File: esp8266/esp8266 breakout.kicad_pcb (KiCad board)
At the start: 2 copper layers, 57.2 x 49.5 mm, 16 parts, among them IC1 DS18B20, P1 power, P3 ftdi, P4 dust, SW1 SW_PUSH, U1 esp8266, U2 AP1117D33

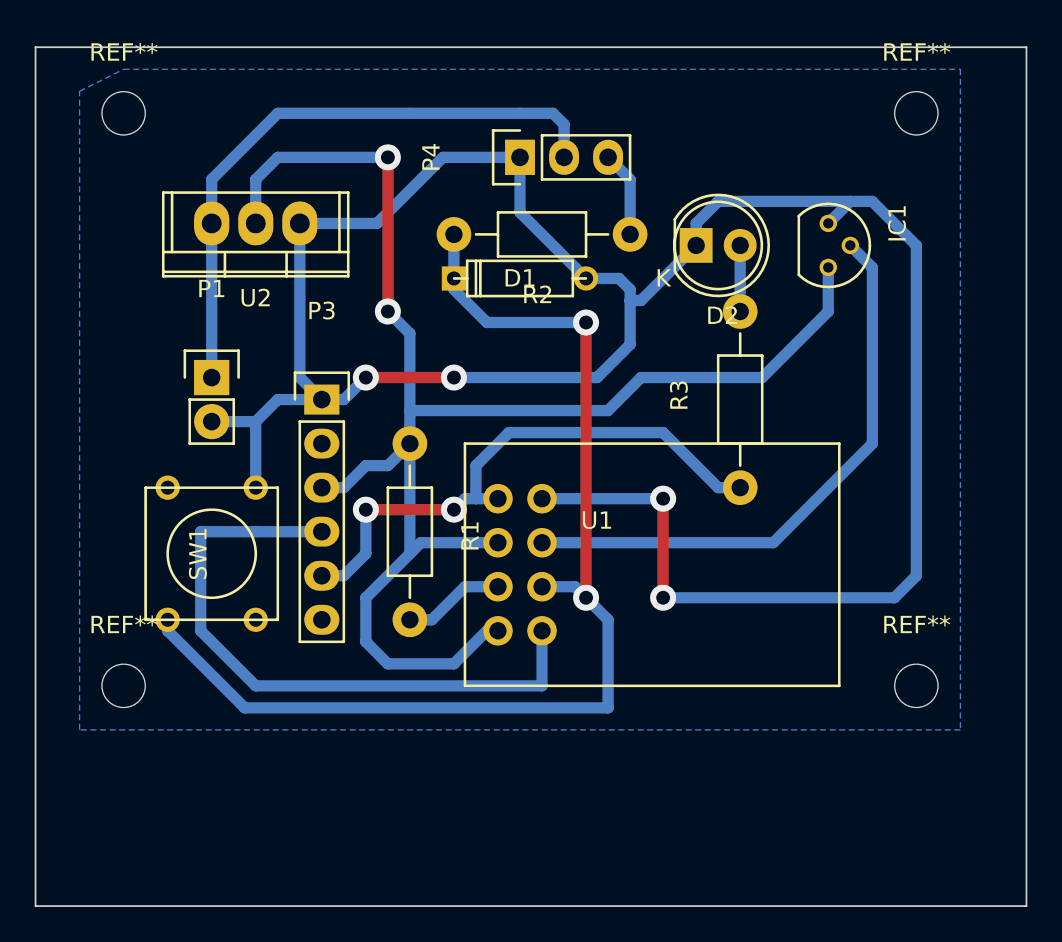
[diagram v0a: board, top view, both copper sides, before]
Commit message: all libs inside project
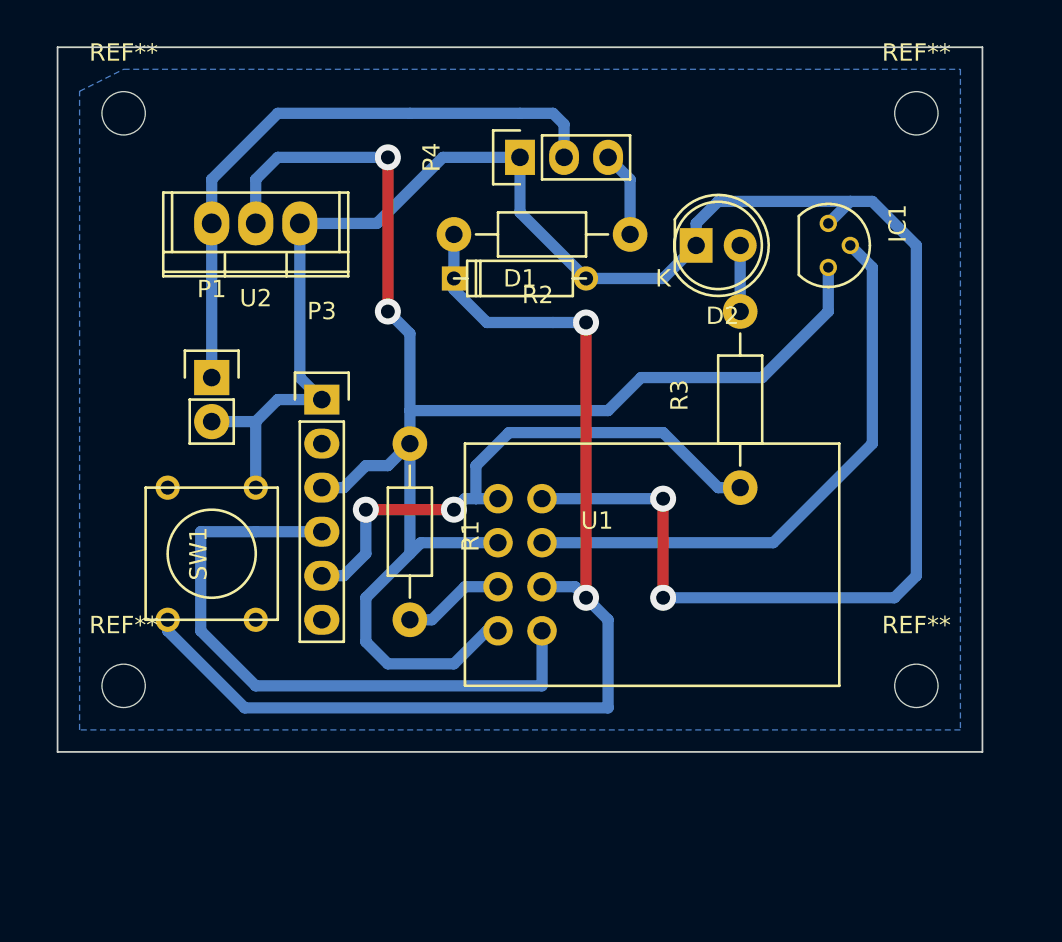
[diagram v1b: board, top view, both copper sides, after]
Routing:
- net GND: track 138.6 -> 115.6 mm, vias 4 -> 2
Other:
- board size 57.2 x 49.5 mm -> 53.3 x 40.6 mm
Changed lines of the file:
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@@
     (links 27)
     (no_connects 2)
-    (area 140.919999 52.019999 198.170001 101.650001)
+    (area 127.255001 39.695 200.453584 93.47418)
     (thickness 1.6)
-    (drawings 4)
-    (tracks 120)
+    (drawings 6)
+    (tracks 109)
     (zones 0)
     (modules 16)
@@
     (pad_drill 0.6)
     (pad_to_mask_clearance 0)
-    (aux_axis_origin 0 0)
+    (aux_axis_origin 146.05 88.9)
     (visible_elements FFFDFF7F)
     (pcbplotparams
@@
       (padsonsilk false)
       (subtractmaskfromsilk false)
-      (outputformat 1)
+      (outputformat 4)
       (mirror false)
       (drillshape 0)
@@
       (effects (font (size 1 1) (thickness 0.15)))
     )
-    (fp_text value MountingHole_2-5mm (at 0.09906 3.59918) (layer F.Fab)
+    (fp_text value MountingHole_2-5mm (at 0 -5.08) (layer F.Fab)
       (effects (font (size 1 1) (thickness 0.15)))
     )
@@
     (pad 1 thru_hole circle (at 0 0) (size 2.5 2.5) (drill 2.5) (layers))
   )
-  (gr_line (start 140.97 101.6) (end 140.97 52.07) (angle 90) (layer Edge.Cuts) (width 0.1))
-  (gr_line (start 198.12 101.6) (end 140.97 101.6) (angle 90) (layer Edge.Cuts) (width 0.1))
-  (gr_line (start 198.12 52.07) (end 198.12 101.6) (angle 90) (layer Edge.Cuts) (width 0.1))
-  (gr_line (start 140.97 52.07) (end 198.12 52.07) (angle 90) (layer Edge.Cuts) (width 0.1))
+  (gr_line (start 142.24 92.71) (end 142.24 52.07) (angle 90) (layer Edge.Cuts) (width 0.1))
+  (gr_line (start 195.58 92.71) (end 142.24 92.71) (angle 90) (layer Edge.Cuts) (width 0.1))
+  (gr_line (start 195.58 52.07) (end 195.58 92.71) (angle 90) (layer Edge.Cuts) (width 0.1))
+  (gr_line (start 142.24 52.07) (end 195.58 52.07) (angle 90) (layer Edge.Cuts) (width 0.1))
+  (dimension 33.02 (width 0.3) (layer F.SilkS)
+    (gr_text "33.020 mm" (at 133.905 72.39 90) (layer F.SilkS)
+      (effects (font (size 1.5 1.5) (thickness 0.3)))
+    )
+    (feature1 (pts (xy 146.05 55.88) (xy 132.555 55.88)))
+    (feature2 (pts (xy 146.05 88.9) (xy 132.555 88.9)))
+    (crossbar (pts (xy 135.255 88.9) (xy 135.255 55.88)))
+    (arrow1a (pts (xy 135.255 55.88) (xy 135.841421 57.006504)))
+    (arrow1b (pts (xy 135.255 55.88) (xy 134.668579 57.006504)))
+    (arrow2a (pts (xy 135.255 88.9) (xy 135.841421 87.773496)))
+    (arrow2b (pts (xy 135.255 88.9) (xy 134.668579 87.773496)))
+  )
+  (dimension 45.72 (width 0.3) (layer F.SilkS)
+    (gr_text "45.720 mm" (at 168.91 41.195) (layer F.SilkS)
+      (effects (font (size 1.5 1.5) (thickness 0.3)))
+    )
+    (feature1 (pts (xy 191.77 55.88) (xy 191.77 39.845)))
+    (feature2 (pts (xy 146.05 55.88) (xy 146.05 39.845)))
+    (crossbar (pts (xy 146.05 42.545) (xy 191.77 42.545)))
+    (arrow1a (pts (xy 191.77 42.545) (xy 190.643496 43.131421)))
+    (arrow1b (pts (xy 191.77 42.545) (xy 190.643496 41.958579)))
+    (arrow2a (pts (xy 146.05 42.545) (xy 147.176504 43.131421)))
+    (arrow2b (pts (xy 146.05 42.545) (xy 147.176504 41.958579)))
+  )
   (segment (start 178.435 71.12) (end 175.895 71.12) (width 0.65) (layer B.Cu) (net 1))
   (segment (start 178.435 71.12) (end 182.88 71.12) (width 0.65) (layer B.Cu) (net 1))
@@
   (segment (start 162.56 68.58) (end 162.56 73.025) (width 0.65) (layer B.Cu) (net 1))
   (segment (start 162.56 73.025) (end 162.56 74.93) (width 0.65) (layer B.Cu) (net 1))
-  (segment (start 175.26 66.675) (end 175.895 66.675) (width 0.65) (layer B.Cu) (net 2))
-  (segment (start 175.895 66.675) (end 179.07 63.5) (width 0.65) (layer B.Cu) (net 2))
+  (segment (start 172.72 65.405) (end 177.165 65.405) (width 0.65) (layer B.Cu) (net 2))
+  (segment (start 177.165 65.405) (end 179.07 63.5) (width 0.65) (layer B.Cu) (net 2))
+  (segment (start 191.77 63.5) (end 191.77 82.55) (width 0.65) (layer B.Cu) (net 2))
   (segment (start 190.5 83.82) (end 177.165 83.82) (width 0.65) (layer B.Cu) (net 2))
   (segment (start 187.96 60.96) (end 189.23 60.96) (width 0.65) (layer B.Cu) (net 2))
   (segment (start 189.23 60.96) (end 191.77 63.5) (width 0.65) (layer B.Cu) (net 2))
-  (segment (start 191.77 63.5) (end 191.77 82.55) (width 0.65) (layer B.Cu) (net 2))
   (segment (start 191.77 82.55) (end 190.5 83.82) (width 0.65) (layer B.Cu) (net 2))
   (via (at 177.165 78.105) (size 1.5) (drill 0.8) (layers F.Cu B.Cu) (net 2))
@@
   (segment (start 160.655 62.23) (end 164.465 58.42) (width 0.65) (layer B.Cu) (net 2))
   (segment (start 160.655 62.23) (end 156.21 62.23) (width 0.65) (layer B.Cu) (net 2))
-  (segment (start 165.1 71.12) (end 173.355 71.12) (width 0.65) (layer B.Cu) (net 2))
-  (segment (start 173.355 71.12) (end 175.26 69.215) (width 0.65) (layer B.Cu) (net 2))
-  (segment (start 175.26 69.215) (end 175.26 66.675) (width 0.65) (layer B.Cu) (net 2))
-  (segment (start 175.26 66.675) (end 175.26 66.04) (width 0.65) (layer B.Cu) (net 2))
-  (segment (start 175.26 66.04) (end 174.625 65.405) (width 0.65) (layer B.Cu) (net 2))
-  (segment (start 174.625 65.405) (end 172.72 65.405) (width 0.65) (layer B.Cu) (net 2))
-  (via (at 165.1 71.12) (size 1.5) (drill 0.8) (layers F.Cu B.Cu) (net 2))
-  (segment (start 165.1 71.12) (end 160.02 71.12) (width 0.65) (layer F.Cu) (net 2))
-  (via (at 160.02 71.12) (size 1.5) (drill 0.8) (layers F.Cu B.Cu) (net 2))
-  (segment (start 160.02 71.12) (end 158.75 72.39) (width 0.65) (layer B.Cu) (net 2))
-  (segment (start 157.48 72.39) (end 158.75 72.39) (width 0.65) (layer B.Cu) (net 2))
   (segment (start 179.07 63.5) (end 179.07 62.23) (width 0.65) (layer B.Cu) (net 2))
+  (segment (start 180.34 60.96) (end 187.96 60.96) (width 0.65) (layer B.Cu) (net 2))
   (segment (start 179.07 62.23) (end 180.34 60.96) (width 0.65) (layer B.Cu) (net 2))
-  (segment (start 180.34 60.96) (end 187.96 60.96) (width 0.65) (layer B.Cu) (net 2))
   (segment (start 186.69 62.23) (end 187.96 60.96) (width 0.65) (layer B.Cu) (net 2))
   (segment (start 151.13 73.66) (end 153.67 73.66) (width 0.65) (layer B.Cu) (net 2))
@@
   (segment (start 171.45 56.515) (end 170.815 55.88) (width 0.65) (layer B.Cu) (net 6))
   (segment (start 151.13 62.23) (end 151.13 71.12) (width 0.65) (layer B.Cu) (net 6))
-  (segment (start 148.59 85.09) (end 148.59 85.725) (width 0.65) (layer B.Cu) (net 7) (status C00000))
-  (segment (start 148.59 85.725) (end 153.035 90.17) (width 0.65) (layer B.Cu) (net 7) (status 400000))
+  (segment (start 148.59 85.09) (end 148.59 85.725) (width 0.65) (layer B.Cu) (net 7))
+  (segment (start 148.59 85.725) (end 153.035 90.17) (width 0.65) (layer B.Cu) (net 7))
   (segment (start 172.72 83.82) (end 173.99 85.09) (width 0.65) (layer B.Cu) (net 7))
   (segment (start 173.99 85.09) (end 173.99 90.17) (width 0.65) (layer B.Cu) (net 7))
